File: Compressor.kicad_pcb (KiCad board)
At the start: 2 copper layers, 56 parts, among them J1 GND 12V, J10 AC LIVE IN, J11 Conn_01x02_Pin, J12 AC OUT 1, J15 Sensor Pins A, J16 Sensor Pins B, J2 GND(A), J3 +12V, J4 Conn_01x02_Pin, J5 Relay In Pins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

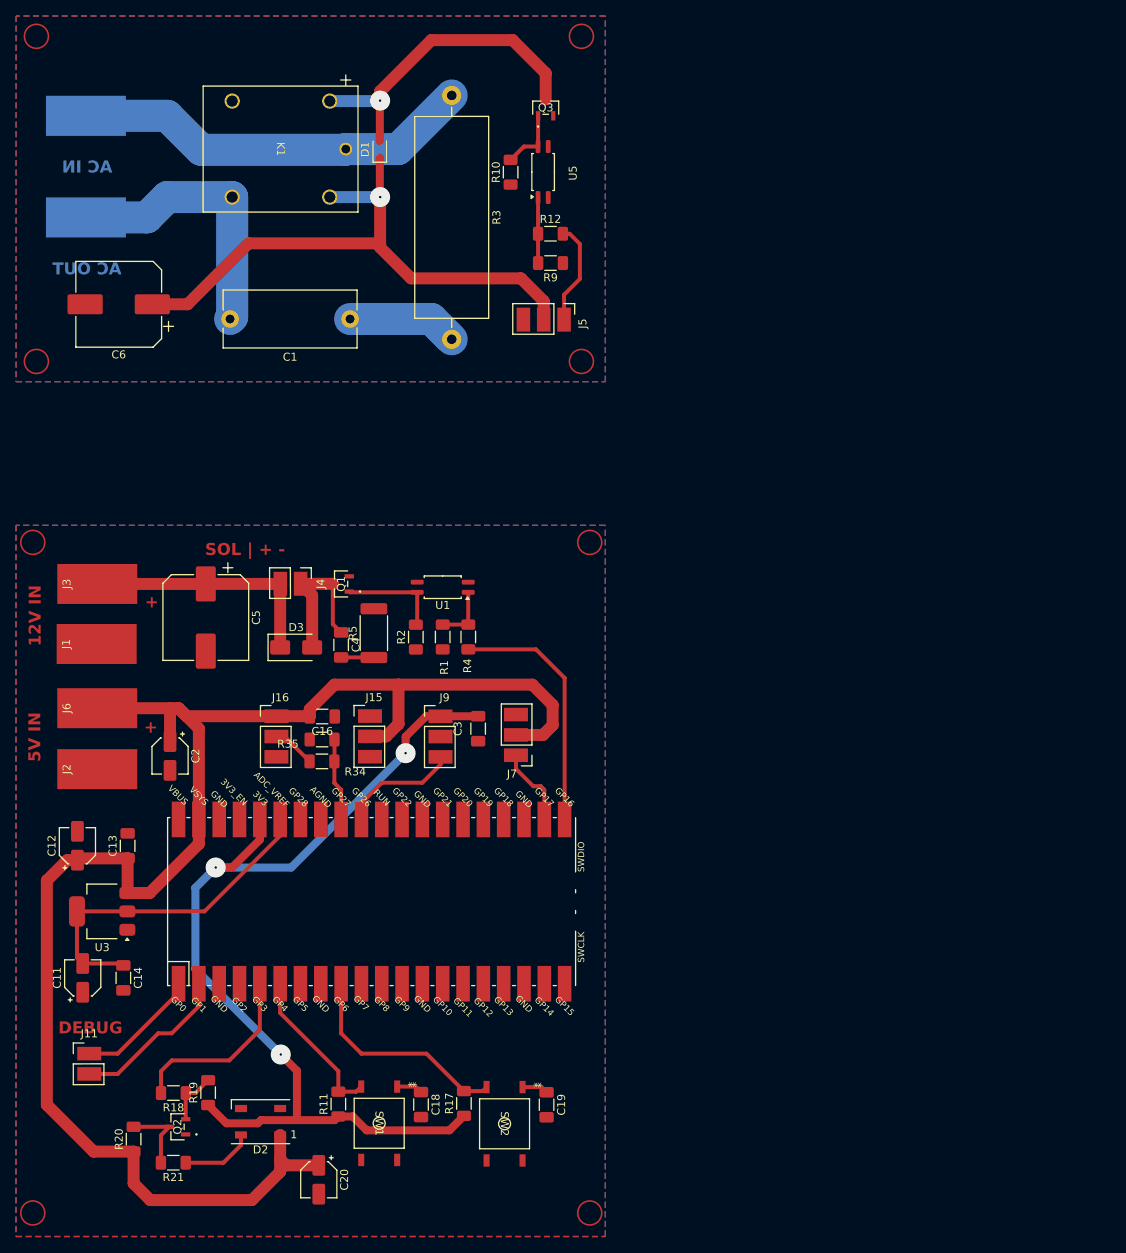
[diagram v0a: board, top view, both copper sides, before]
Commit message: Split up boards
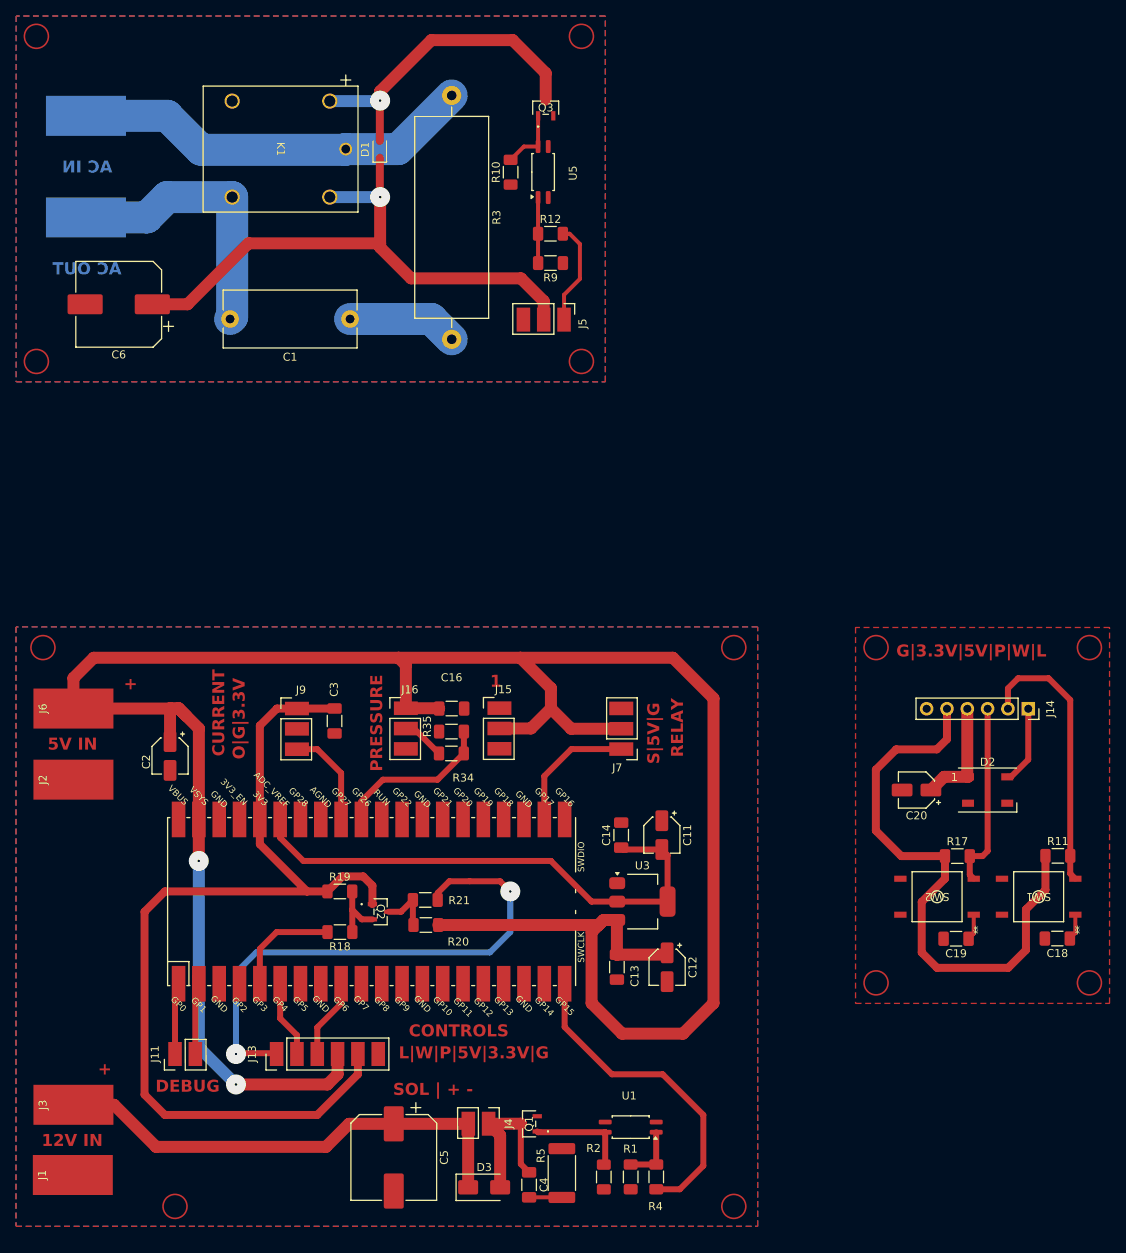
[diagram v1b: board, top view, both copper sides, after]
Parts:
- added J13: Conn_01x06_Pin, SMD-Connectors:SMD-PinHeader_1x06_P2.54mm_Vertical, F.Cu at (54.7, 158.7)
- added J14: Conn_01x06_Pin, Connector_PinSocket_2.54mm:PinSocket_1x06_P2.54mm_Vertical, F.Cu at (142.2, 115.6)
- moved D2 99.9 mm to (137.1, 125.8), turned to 0 degrees
- moved R11 95.1 mm to (145.9, 134.0), turned to 0 degrees
- moved C20 89.2 mm to (128.2, 125.8), turned to 180 degrees
- moved SW1 87.2 mm to (143.5, 139.1), turned to 180 degrees
- moved C18 82.2 mm to (145.9, 144.3), turned to 180 degrees
- moved C12 75.3 mm to (97.1, 147.9), turned to -90 degrees
- moved C11 74.6 mm to (96.4, 131.4), turned to -90 degrees
- moved C5 71.5 mm to (62.9, 171.7)
- moved D3 71.5 mm to (74.2, 175.4)
- moved J4 71.5 mm to (74.8, 168.0)
- moved R5 71.5 mm to (83.9, 173.6)
- moved U1 71.5 mm to (92.5, 167.9)
- moved C4 71.5 mm to (79.8, 175.1)
- moved Q1 71.5 mm to (79.8, 167.5)
- moved R1 71.5 mm to (92.5, 174.1)
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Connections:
- R11 pad 2: /Reset Wifi -> Net-(J14-Pin_2)
- R17 pad 2: /Shut Down -> Net-(J14-Pin_3)
- R21 pad 1: Net-(D2-DIN) -> Net-(J13-Pin_1)
- SW1 pad 2: /Reset Wifi -> Net-(J14-Pin_2)
- SW2 pad 2: /Shut Down -> Net-(J14-Pin_3)
- U6 pad 20: unconnected-(U6-GPIO15-Pad20) -> /Solenoid
- U6 pad 21: /Solenoid -> unconnected-(U6-GPIO16-Pad21)
- U6 pad 31: /Current Sense -> /Pressure
- U6 pad 32: /Pressure -> /Current Sense
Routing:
- net +5V(A): track 277.0 -> 397.1 mm, vias 1 -> 3
- net +3.3V: track 122.6 -> 194.4 mm, vias 3 -> 0
- net Net-(J13-Pin_1): track 0.00 -> 67.8 mm, vias 0 -> 2
- net Net-(J14-Pin_2): track 0.00 -> 34.6 mm
- net +12V: track 30.9 -> 60.7 mm
- net Net-(J14-Pin_3): track 0.00 -> 23.3 mm
- net Net-(U3-VO): track 43.0 -> 64.6 mm
- net /Shut Down: track 29.0 -> 11.3 mm
- net /RGB LED: track 24.4 -> 12.3 mm
- net Net-(J11-Pin_2): track 21.4 -> 10.3 mm
- net /Reset Wifi: track 21.0 -> 10.9 mm
- net /Pressure: track 11.7 -> 21.7 mm
- net /Solenoid: track 32.6 -> 42.1 mm
- net Net-(J11-Pin_1): track 16.8 -> 10.3 mm
- net /Relay 1: track 11.4 -> 17.8 mm
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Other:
- board text added: "1"
- board text added: "CONTROLS"
- board text added: "CURRENT"
- board text added: "G|3.3V|5V|P|W|L"
- board text added: "L|W|P|5V|3.3V|G"
- board text added: "O|G|3.3V"
- board text added: "PRESSURE"
- board text added: "RELAY"
- board text added: "S|5V|G"

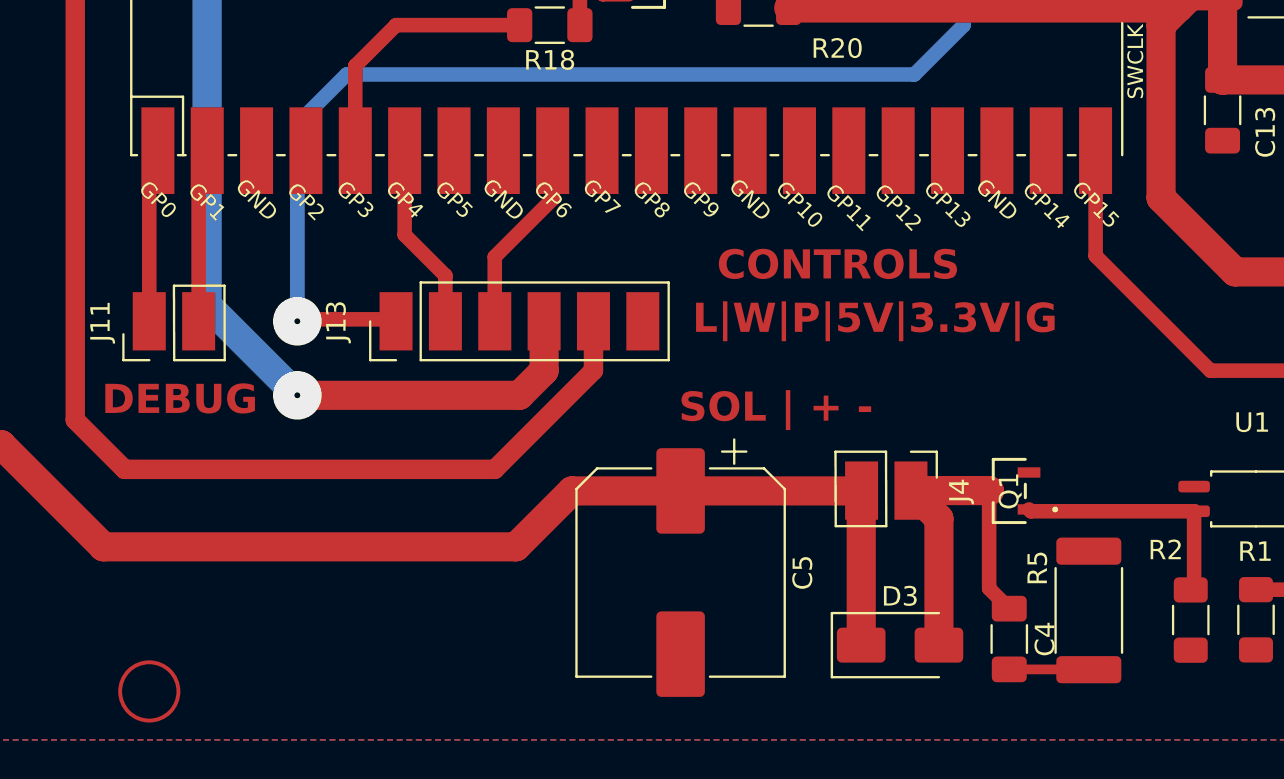
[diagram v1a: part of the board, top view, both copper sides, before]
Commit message: Added temp sensor
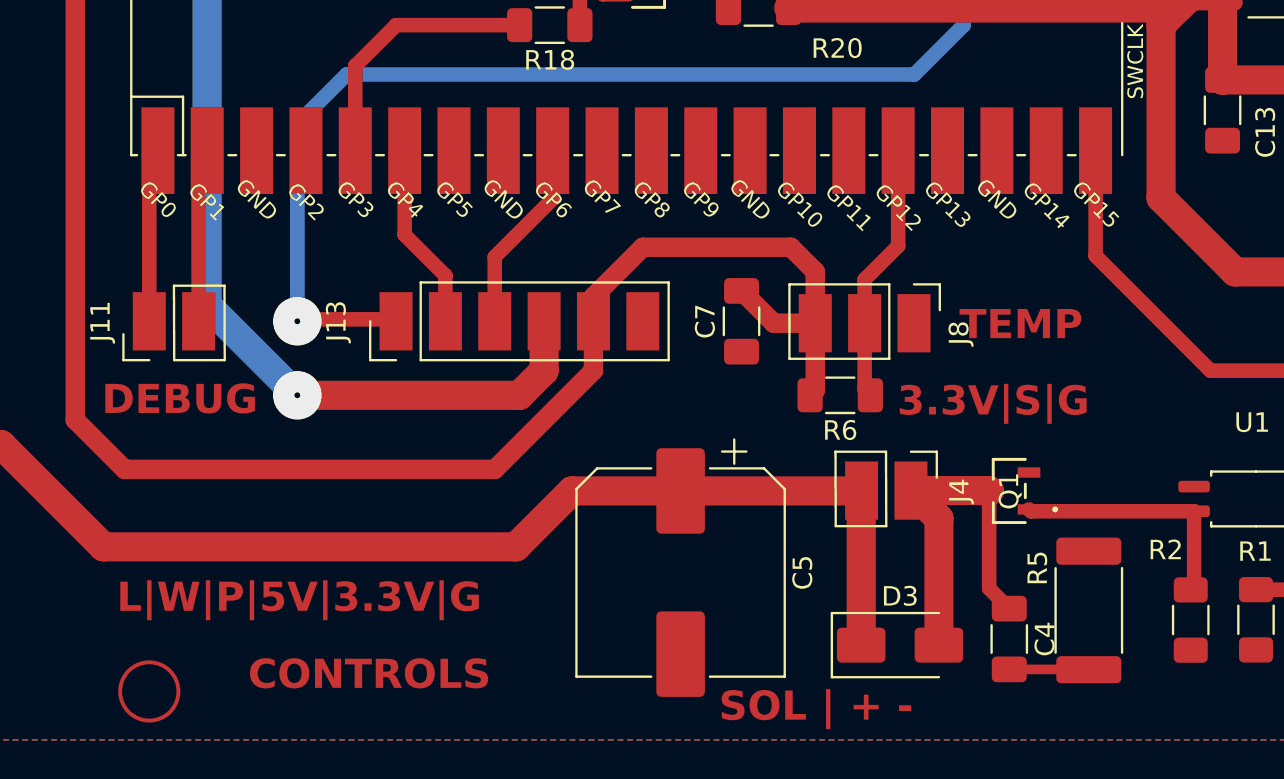
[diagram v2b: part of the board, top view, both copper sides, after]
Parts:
- added C7: 100nf, Capacitor_SMD:C_1206_3216Metric_Pad1.33x1.80mm_HandSolder, F.Cu at (66.0, 158.8)
- added J8: Temp sensor out pins, SMD-Connectors:SMD-PinHeader_1x03_P2.54mm_Vertical, F.Cu at (74.9, 159.3)
- added R6: 4K7, Resistor_SMD:R_1206_3216Metric_Pad1.30x1.75mm_HandSolder, F.Cu at (71.1, 162.6)
- J13: value Conn_01x06_Pin -> Controlls Connector
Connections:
- U6 pad 16: unconnected-(U6-GPIO12-Pad16) -> Net-(J8-Pin_2)
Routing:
- net +3.3V: track 194.4 -> 219.6 mm
- net Net-(J8-Pin_2): track 0.00 -> 14.8 mm
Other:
- board text added: "3.3V|S|G"
- board text added: "TEMP"
